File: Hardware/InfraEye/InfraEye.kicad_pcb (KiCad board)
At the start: 2 copper layers, 8 parts, among them Q1 Q_NPN_BCE, U1 MLX90640, U2 ESP32-WROOM-32, U3 TFT_SPI_24_LCD

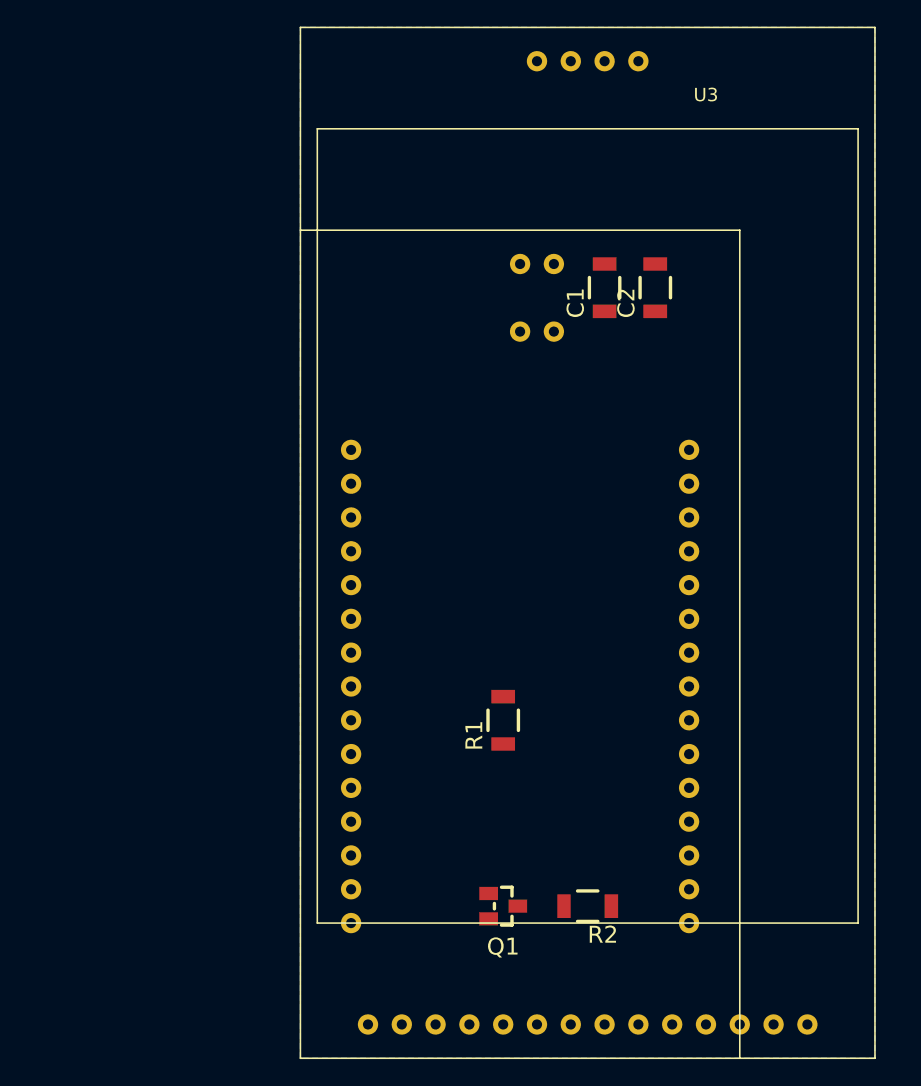
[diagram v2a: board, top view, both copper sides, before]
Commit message: PCB: Added second IR sensor - LCD/WIFI version will have IR sensor placed on different places of PCB. SW: Changed pins of SPI buses, LCD moved to VSPI bus and speed increased to 60MHz, touch sensor moved to HSPI bus and speed decreased to 125kHz. Some changes done to reading from touch sensor, some data that correspond to screen touching are present on bus, but data still doesn't give coordinates.
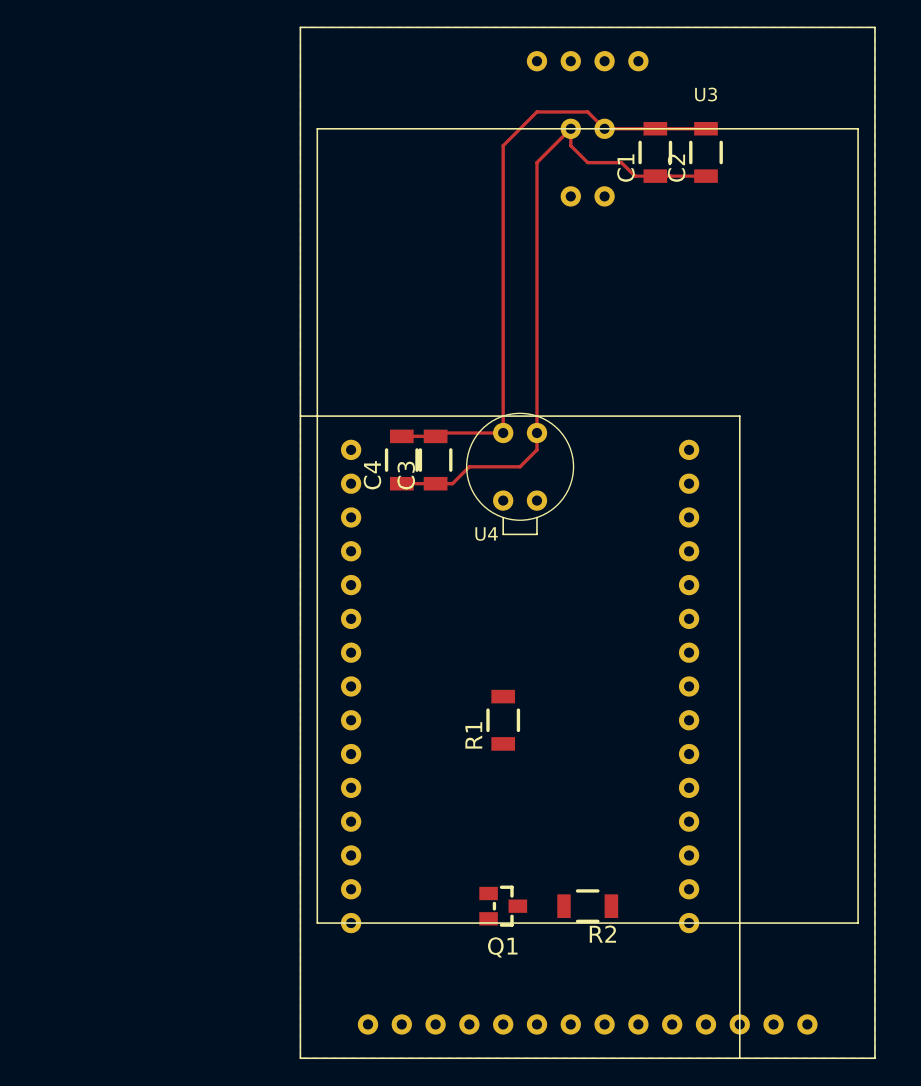
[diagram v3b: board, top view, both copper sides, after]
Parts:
- added C3: 10nF, OLIMEX_RLC-FP:C_1206_5MIL_DWS_ISO, F.Cu at (116.8, 73.2)
- added C4: 100nF, OLIMEX_RLC-FP:C_1206_5MIL_DWS_ISO, F.Cu at (114.3, 73.2)
- added U4: MLX90640, InfraEye:MLX90614, F.Cu at (124.5, 76.2)
- moved C1 10.9 mm to (133.3, 50.0)
- moved C2 10.9 mm to (137.2, 50.0)
- moved U1 10.9 mm to (127.0, 53.3)
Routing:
- net Net-(C1-Pad1): track 0.00 -> 48.8 mm
- net GND: track 0.00 -> 46.1 mm
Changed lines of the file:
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@@
     (thickness 1.6)
     (drawings 2)
-    (tracks 0)
+    (tracks 25)
     (zones 0)
-    (modules 8)
+    (modules 11)
     (nets 43)
   )
@@
   )
   (module OLIMEX_RLC-FP:C_1206_5MIL_DWS_ISO (layer F.Cu)
-    (at 129.54 60.198 90)
+    (at 133.35 50.038 90)
     (attr smd)
     (fp_text reference C1 (at -1.143 -2.159 90) (layer F.SilkS)
@@
   )
   (module OLIMEX_RLC-FP:C_1206_5MIL_DWS_ISO (layer F.Cu)
-    (at 133.35 60.198 90)
+    (at 137.16 50.038 90)
     (attr smd)
     (fp_text reference C2 (at -1.143 -2.159 90) (layer F.SilkS)
@@
   )
   (module InfraEye:MLX90614 (layer B.Cu)
-    (at 123.19 63.5)
+    (at 127 53.34)
     (fp_text reference U1 (at 3.81 2.54) (layer B.SilkS)
       (effects (font (size 1 1) (thickness 0.15)) (justify mirror))
@@
     )
   )
-  (gr_line (start 139.7 55.88) (end 139.7 118.11) (layer F.SilkS) (width 0.12))
-  (gr_line (start 106.68 55.88) (end 139.7 55.88) (layer F.SilkS) (width 0.12))
+  (module OLIMEX_RLC-FP:C_1206_5MIL_DWS_ISO (layer F.Cu)
+    (at 116.84 73.152 90)
+    (attr smd)
+    (fp_text reference C3 (at -1.143 -2.159 90) (layer F.SilkS)
+      (effects (font (size 1.27 1.27) (thickness 0.254)))
+    )
+    (fp_text value 10nF (at 0.127 2.286 90) (layer F.Fab)
+      (effects (font (size 1.27 1.27) (thickness 0.254)))
+    )
+    (fp_line (start 1.651 0.762) (end 1.651 -0.762) (layer F.Fab) (width 0.15))
+    (fp_line (start -1.651 0.762) (end 1.651 0.762) (layer F.Fab) (width 0.15))
+    (fp_line (start -1.651 -0.762) (end -1.651 0.762) (layer F.Fab) (width 0.15))
+    (fp_line (start -1.651 -0.762) (end 1.651 -0.762) (layer F.Fab) (width 0.15))
+    (fp_line (start 0.762 -1.143) (end 2.413 -1.143) (layer Dwgs.User) (width 0.254))
+    (fp_line (start 2.413 -1.143) (end 2.413 1.143) (layer Dwgs.User) (width 0.254))
+    (fp_line (start 2.413 1.143) (end 0.762 1.143) (layer Dwgs.User) (width 0.254))
+    (fp_line (start -0.762 -1.143) (end -2.413 -1.143) (layer Dwgs.User) (width 0.254))
+    (fp_line (start -2.413 -1.143) (end -2.413 1.143) (layer Dwgs.User) (width 0.254))
+    (fp_line (start -2.413 1.143) (end -0.762 1.143) (layer Dwgs.User) (width 0.254))
+    (fp_line (start 0.762 1.143) (end -0.762 1.143) (layer F.SilkS) (width 0.254))
+    (fp_line (start 0.762 -1.143) (end -0.762 -1.143) (layer F.SilkS) (width 0.254))
+    (pad 1 smd rect (at -1.778 0 90) (size 1.016 1.778) (layers F.Cu F.Paste F.Mask)
+      (net 2 "Net-(C1-Pad1)") (solder_mask_margin 0.0508))
+    (pad 2 smd rect (at 1.778 0 90) (size 1.016 1.778) (layers F.Cu F.Paste F.Mask)
+      (net 3 GND) (solder_mask_margin 0.0508))
+    (model ${KISYS3DMOD}/C_1206_3216Metric.wrl
+      (at (xyz 0 0 0))
+      (scale (xyz 1 1 1))
+      (rotate (xyz 0 0 0))
+    )
+  )
+  (module OLIMEX_RLC-FP:C_1206_5MIL_DWS_ISO (layer F.Cu)
+    (at 114.3 73.152 90)
+    (attr smd)
+    (fp_text reference C4 (at -1.143 -2.159 90) (layer F.SilkS)
+      (effects (font (size 1.27 1.27) (thickness 0.254)))
+    )
+    (fp_text value 100nF (at 0.127 2.286 90) (layer F.Fab)
+      (effects (font (size 1.27 1.27) (thickness 0.254)))
+    )
+    (fp_line (start 0.762 -1.143) (end -0.762 -1.143) (layer F.SilkS) (width 0.254))
+    (fp_line (start 0.762 1.143) (end -0.762 1.143) (layer F.SilkS) (width 0.254))
+    (fp_line (start -2.413 1.143) (end -0.762 1.143) (layer Dwgs.User) (width 0.254))
+    (fp_line (start -2.413 -1.143) (end -2.413 1.143) (layer Dwgs.User) (width 0.254))
+    (fp_line (start -0.762 -1.143) (end -2.413 -1.143) (layer Dwgs.User) (width 0.254))
+    (fp_line (start 2.413 1.143) (end 0.762 1.143) (layer Dwgs.User) (width 0.254))
+    (fp_line (start 2.413 -1.143) (end 2.413 1.143) (layer Dwgs.User) (width 0.254))
+    (fp_line (start 0.762 -1.143) (end 2.413 -1.143) (layer Dwgs.User) (width 0.254))
+    (fp_line (start -1.651 -0.762) (end 1.651 -0.762) (layer F.Fab) (width 0.15))
+    (fp_line (start -1.651 -0.762) (end -1.651 0.762) (layer F.Fab) (width 0.15))
+    (fp_line (start -1.651 0.762) (end 1.651 0.762) (layer F.Fab) (width 0.15))
+    (fp_line (start 1.651 0.762) (end 1.651 -0.762) (layer F.Fab) (width 0.15))
+    (pad 2 smd rect (at 1.778 0 90) (size 1.016 1.778) (layers F.Cu F.Paste F.Mask)
+      (net 3 GND) (solder_mask_margin 0.0508))
+    (pad 1 smd rect (at -1.778 0 90) (size 1.016 1.778) (layers F.Cu F.Paste F.Mask)
+      (net 2 "Net-(C1-Pad1)") (solder_mask_margin 0.0508))
+    (model ${KISYS3DMOD}/C_1206_3216Metric.wrl
+      (at (xyz 0 0 0))
+      (scale (xyz 1 1 1))
+      (rotate (xyz 0 0 0))
+    )
+  )
+  (module InfraEye:MLX90614 (layer F.Cu)
+    (at 124.46 76.2 180)
+    (fp_text reference U4 (at 3.81 -2.54) (layer F.SilkS)
+      (effects (font (size 1 1) (thickness 0.15)))
+    )
+    (fp_text value MLX90640 (at 1.27 -3.81) (layer F.Fab)
+      (effects (font (size 1 1) (thickness 0.15)))
+    )
+    (fp_circle (center 1.27 2.54) (end 5.08 3.81) (layer F.SilkS) (width 0.1))
+    (fp_line (start 0 -1.27) (end 0 -2.54) (layer F.SilkS) (width 0.12))
+    (fp_line (start 0 -2.54) (end 2.54 -2.54) (layer F.SilkS) (width 0.12))
+    (fp_line (start 2.54 -2.54) (end 2.54 -1.27) (layer F.SilkS) (width 0.12))
+    (pad 1 thru_hole circle (at 0 0 180) (size 1.524 1.524) (drill 0.762) (layers *.Cu *.Mask)
+      (net 1 "Net-(U1-Pad1)"))
+    (pad 2 thru_hole circle (at 0 5.08 180) (size 1.524 1.524) (drill 0.762) (layers *.Cu *.Mask)
+      (net 2 "Net-(C1-Pad1)"))
+    (pad 3 thru_hole circle (at 2.54 5.08 180) (size 1.524 1.524) (drill 0.762) (layers *.Cu *.Mask)
+      (net 3 GND))
+    (pad 4 thru_hole circle (at 2.54 0 180) (size 1.524 1.524) (drill 0.762) (layers *.Cu *.Mask)
+      (net 4 "Net-(U1-Pad4)"))
+    (model ${OLIMEXFOOTPATH}/OLIMEX_3Dmodels/MLX90614.step
+      (at (xyz 0 0 0))
+      (scale (xyz 1 1 1))
+      (rotate (xyz 0 0 -45))
+    )
+  )
+  (gr_line (start 139.7 69.85) (end 139.7 118.11) (layer F.SilkS) (width 0.12))
+  (gr_line (start 106.68 69.85) (end 139.7 69.85) (layer F.SilkS) (width 0.12))
+  (segment (start 127 48.26) (end 127 49.53) (width 0.25) (layer F.Cu) (net 2))
+  (segment (start 127 49.53) (end 128.27 50.8) (width 0.25) (layer F.Cu) (net 2))
+  (segment (start 128.27 50.8) (end 130.81 50.8) (width 0.25) (layer F.Cu) (net 2))
+  (segment (start 131.826 51.816) (end 133.35 51.816) (width 0.25) (layer F.Cu) (net 2))
+  (segment (start 130.81 50.8) (end 131.826 51.816) (width 0.25) (layer F.Cu) (net 2))
+  (segment (start 134.489 51.816) (end 137.16 51.816) (width 0.25) (layer F.Cu) (net 2))
+  (segment (start 133.35 51.816) (end 134.489 51.816) (width 0.25) (layer F.Cu) (net 2))
+  (segment (start 114.3 74.93) (end 116.84 74.93) (width 0.25) (layer F.Cu) (net 2))
+  (segment (start 124.46 72.39) (end 124.46 71.12) (width 0.25) (layer F.Cu) (net 2))
+  (segment (start 123.19 73.66) (end 124.46 72.39) (width 0.25) (layer F.Cu) (net 2))
+  (segment (start 119.38 73.66) (end 123.19 73.66) (width 0.25) (layer F.Cu) (net 2))
+  (segment (start 116.84 74.93) (end 118.11 74.93) (width 0.25) (layer F.Cu) (net 2))
+  (segment (start 118.11 74.93) (end 119.38 73.66) (width 0.25) (layer F.Cu) (net 2))
+  (segment (start 124.46 50.8) (end 127 48.26) (width 0.25) (layer F.Cu) (net 2))
+  (segment (start 124.46 71.12) (end 124.46 50.8) (width 0.25) (layer F.Cu) (net 2))
+  (segment (start 129.54 48.26) (end 133.35 48.26) (width 0.25) (layer F.Cu) (net 3))
+  (segment (start 137.16 48.26) (end 133.35 48.26) (width 0.25) (layer F.Cu) (net 3))
+  (segment (start 117.094 71.12) (end 116.84 71.374) (width 0.25) (layer F.Cu) (net 3))
+  (segment (start 121.92 71.12) (end 117.094 71.12) (width 0.25) (layer F.Cu) (net 3))
+  (segment (start 115.439 71.374) (end 116.84 71.374) (width 0.25) (layer F.Cu) (net 3))
+  (segment (start 114.3 71.374) (end 115.439 71.374) (width 0.25) (layer F.Cu) (net 3))
+  (segment (start 121.92 71.12) (end 121.92 49.53) (width 0.25) (layer F.Cu) (net 3))
+  (segment (start 121.92 49.53) (end 124.46 46.99) (width 0.25) (layer F.Cu) (net 3))
+  (segment (start 128.27 46.99) (end 129.54 48.26) (width 0.25) (layer F.Cu) (net 3))
+  (segment (start 124.46 46.99) (end 128.27 46.99) (width 0.25) (layer F.Cu) (net 3))
   (zone (net 3) (net_name GND) (layer B.Cu) (hatch edge 0.508)
     (connect_pads (clearance 0.508))
     (min_thickness 0.254)
-    (fill yes (arc_segments 32) (thermal_gap 0.508) (thermal_bridge_width 0.508))
+    (fill (arc_segments 32) (thermal_gap 0.508) (thermal_bridge_width 0.508))
     (polygon
       (pts

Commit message: Reworked schematics and PCB - signals moved around to minimize signal crossings - not verified on HW if it works with remapped signals as on schematics.
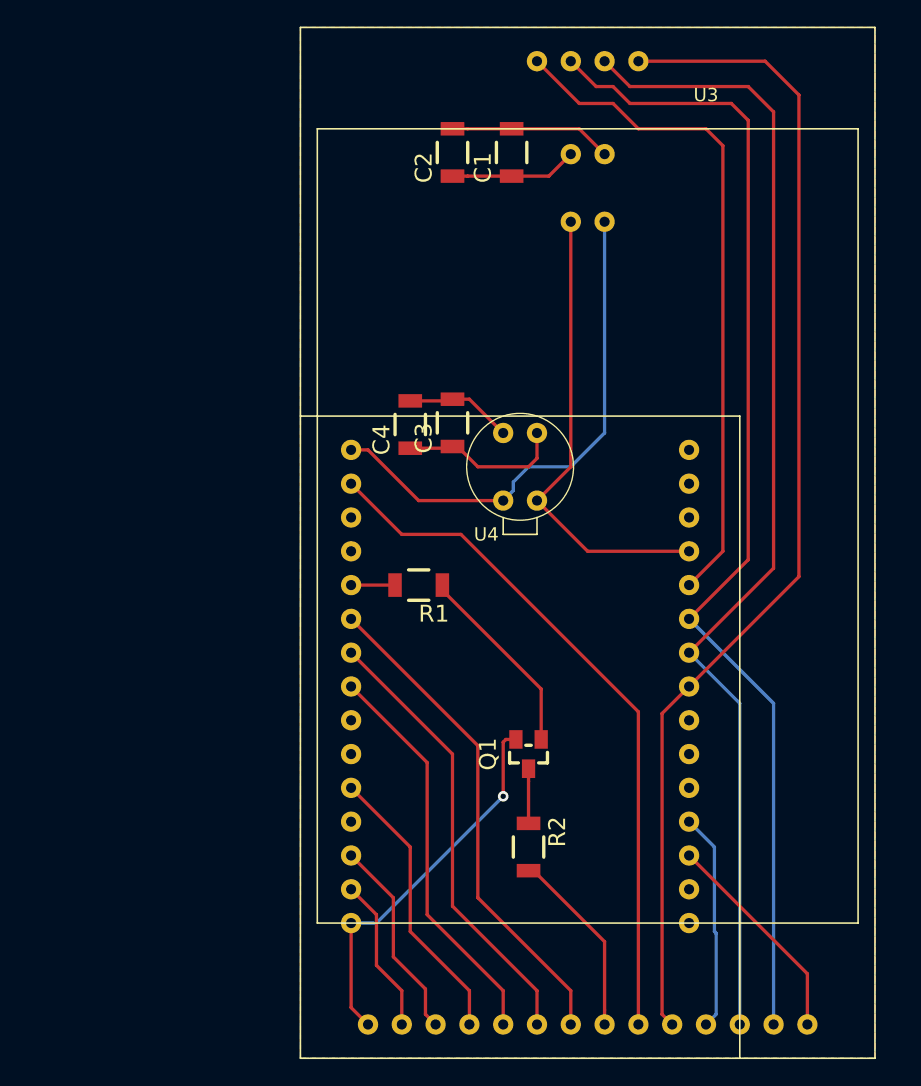
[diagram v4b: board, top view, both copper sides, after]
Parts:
- moved C2 19.0 mm to (118.1, 50.0)
- moved R1 12.0 mm to (115.6, 82.5), turned to 180 degrees
- moved Q1 11.6 mm to (123.8, 95.2), turned to 90 degrees
- moved C1 10.8 mm to (122.6, 50.0)
- moved R2 6.29 mm to (123.8, 102.2), turned to 270 degrees
- moved C3 3.07 mm to (118.1, 70.4)
- moved C4 2.74 mm to (114.9, 70.5)
- moved U1 1.90 mm to (127.0, 55.2)
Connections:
- net Net-(C1-Pad1) renamed +3V3
- R2 pad 1: Net-(R2-Pad1) -> Net-(Q1-Pad3)
- R2 pad 2: Net-(Q1-Pad3) -> Net-(R2-Pad2)
- U2 pad 12: Net-(U2-Pad12) -> Net-(U1-Pad1)
- U2 pad 2: Net-(U2-Pad2) -> GND
- U2 pad 23: Net-(R1-Pad2) -> Net-(U2-Pad23)
- U2 pad 26: Net-(U2-Pad26) -> Net-(R1-Pad2)
- U2 pad 3: Net-(U1-Pad4) -> Net-(U2-Pad3)
- U2 pad 30: Net-(U2-Pad30) -> Net-(U1-Pad4)
- U2 pad 4: Net-(U1-Pad1) -> Net-(U2-Pad4)
- U3 pad 10: Net-(U3-Pad10) -> Net-(U2-Pad8)
- U3 pad 11: Net-(U3-Pad11) -> Net-(U2-Pad4)
- U3 pad 12: Net-(U3-Pad12) -> Net-(U2-Pad9)
- U3 pad 13: Net-(U3-Pad13) -> Net-(U2-Pad10)
- U3 pad 14: Net-(U3-Pad14) -> Net-(U2-Pad3)
- U3 pad 15: Net-(U3-Pad15) -> Net-(U2-Pad11)
- U3 pad 16: Net-(U3-Pad16) -> Net-(U2-Pad10)
- U3 pad 17: Net-(U3-Pad17) -> Net-(U2-Pad9)
- U3 pad 18: Net-(U3-Pad18) -> Net-(U2-Pad8)
- U3 pad 3: Net-(U2-Pad29) -> Net-(U2-Pad18)
- U3 pad 4: Net-(U2-Pad24) -> Net-(U2-Pad20)
- U3 pad 5: Net-(U2-Pad26) -> Net-(U2-Pad23)
- U3 pad 6: Net-(U2-Pad30) -> Net-(U2-Pad24)
- U3 pad 8: Net-(R2-Pad1) -> Net-(R2-Pad2)
- U3 pad 9: Net-(U2-Pad8) -> Net-(U2-Pad29)
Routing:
- net Net-(U2-Pad10): track 0.00 -> 87.6 mm
- net Net-(U2-Pad8): track 0.00 -> 87.5 mm
- net Net-(U2-Pad9): track 0.00 -> 87.1 mm
- net Net-(U2-Pad29): track 0.00 -> 52.2 mm
- net Net-(U2-Pad11): track 0.00 -> 51.3 mm
- net Net-(U1-Pad4): track 0.00 -> 39.0 mm
- net Net-(U2-Pad25): track 0.00 -> 37.3 mm
- net Net-(U1-Pad1): track 0.00 -> 35.0 mm
- net Net-(U2-Pad24): track 0.00 -> 33.7 mm
- net Net-(U2-Pad23): track 0.00 -> 30.1 mm
- net Net-(U2-Pad20): track 0.00 -> 21.5 mm
- net Net-(U2-Pad4): track 0.00 -> 16.4 mm
- net Net-(U2-Pad3): track 0.00 -> 16.4 mm
- net Net-(U2-Pad18): track 0.00 -> 15.3 mm
- net Net-(Q1-Pad1): track 0.00 -> 14.7 mm
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- added copper zone on F.Cu, net +3V3
